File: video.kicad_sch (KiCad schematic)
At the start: 4 parts, among them J1 Video Output Female, J2 Board Interconnect Female, J3 Conn_02x08_Odd_Even

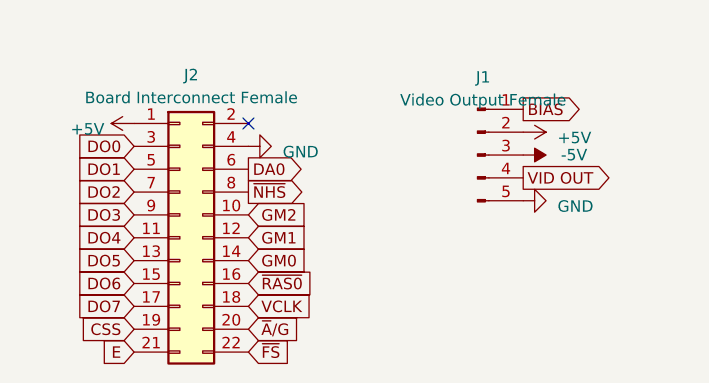
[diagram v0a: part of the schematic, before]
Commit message: redo layout for SAMx8
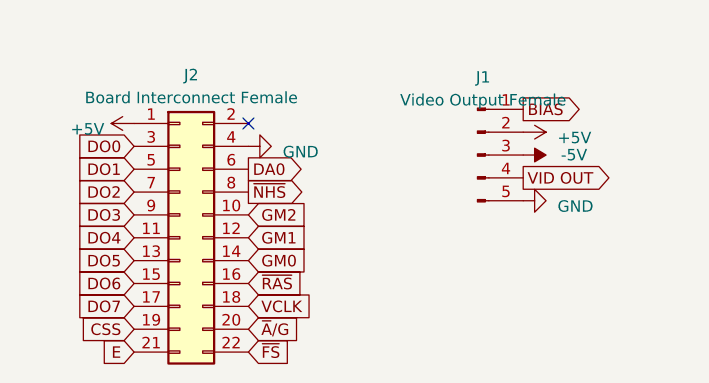
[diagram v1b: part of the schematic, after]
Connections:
- net ~{RAS0} renamed ~{RAS}
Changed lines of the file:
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@@
 		)
 	)
-	(global_label "~{RAS0}"
+	(global_label "~{RAS}"
 		(shape input)
 		(at 137.1092 183.1848 0)
@@
 		)
 		(property "Intersheetrefs" "${INTERSHEET_REFS}"
-			(at 144.1384 183.1848 0)
+			(at 143.0083 183.1848 0)
 			(effects
 				(font

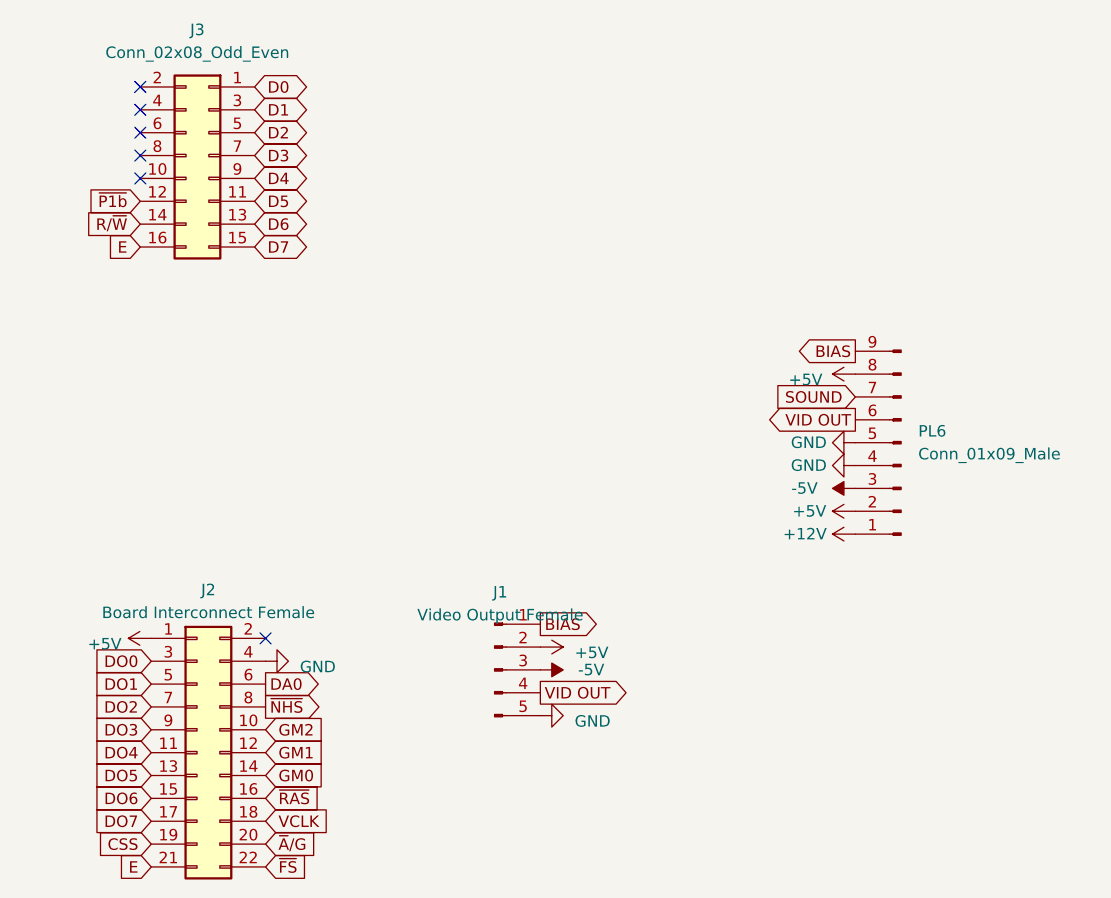
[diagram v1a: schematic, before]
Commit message: include CUPL for keyboard GAL
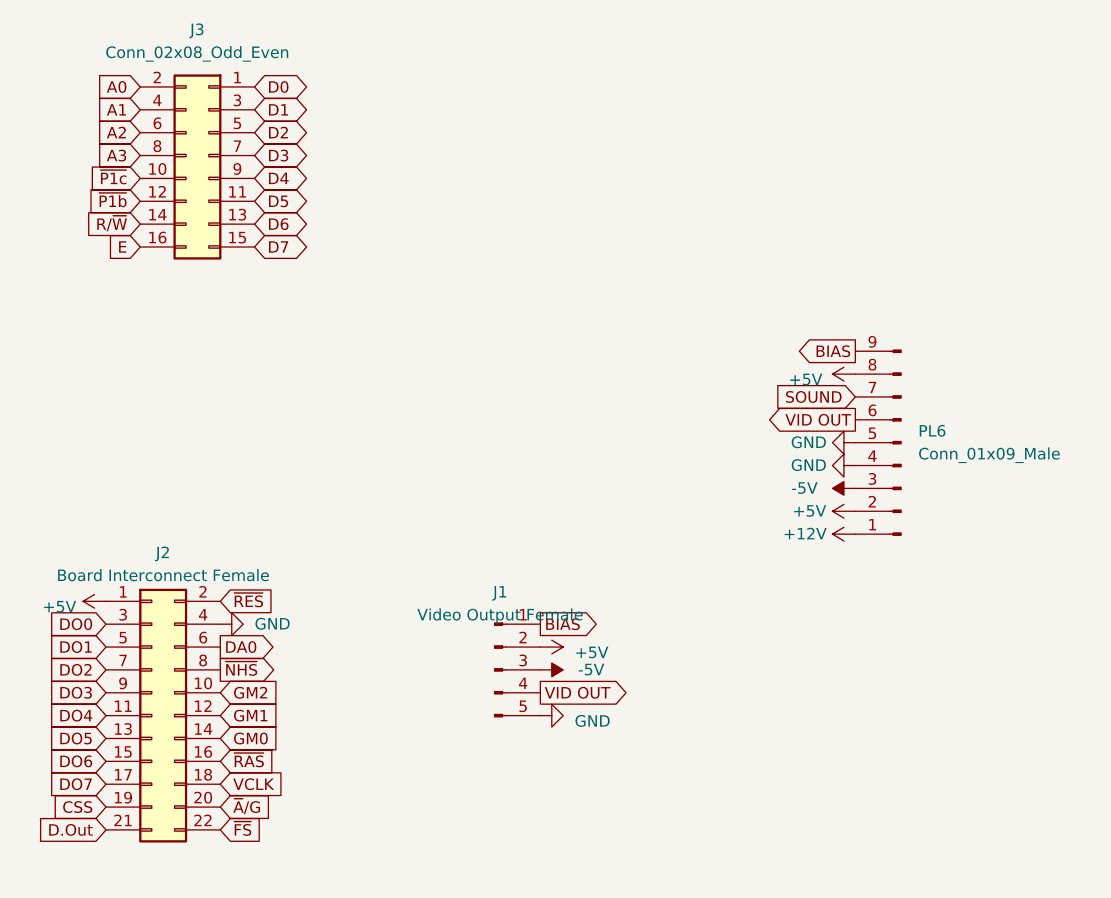
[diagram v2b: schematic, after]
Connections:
- net E: no longer J2.21 (Pin_21)
- net ~{RES}: now reaches J2.2 (Pin_2)
- net ~{P1c}: now reaches J3.10 (Pin_10)
- net A0: now reaches J3.2 (Pin_2)
- net A1: now reaches J3.4 (Pin_4)
- net A2: now reaches J3.6 (Pin_6)
- net A3: now reaches J3.8 (Pin_8)
- new net D.Out: J2.21 (Pin_21)
- no-connect marks 6 -> 0
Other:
- moved on the sheet: J2

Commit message: align versions
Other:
- title: (none) -> Dragon CPU UK Revised
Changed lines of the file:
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@@
 	(paper "A3")
 	(title_block
-		(date "2023-05-25")
-		(rev "3.0")
+		(title "Dragon CPU UK Revised")
+		(date "2025-10-05")
+		(rev "3.3")
+		(comment 1 "Redesign by Julian Brown")
 		(comment 2 "Reposition dram and buffer")
 	)
